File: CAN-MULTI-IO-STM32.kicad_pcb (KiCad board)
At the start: 2 copper layers, 81 x 55 mm, 63 parts, among them J1 H GND L, J2 TERM, J3 USART1, J5 PWR IN, U1 STM32L433RCT3, U2 MCP2562-E-SN, U3 LMR54410, U4 ADS1015IDGS, U5 PCA9537, U6 TCA9511

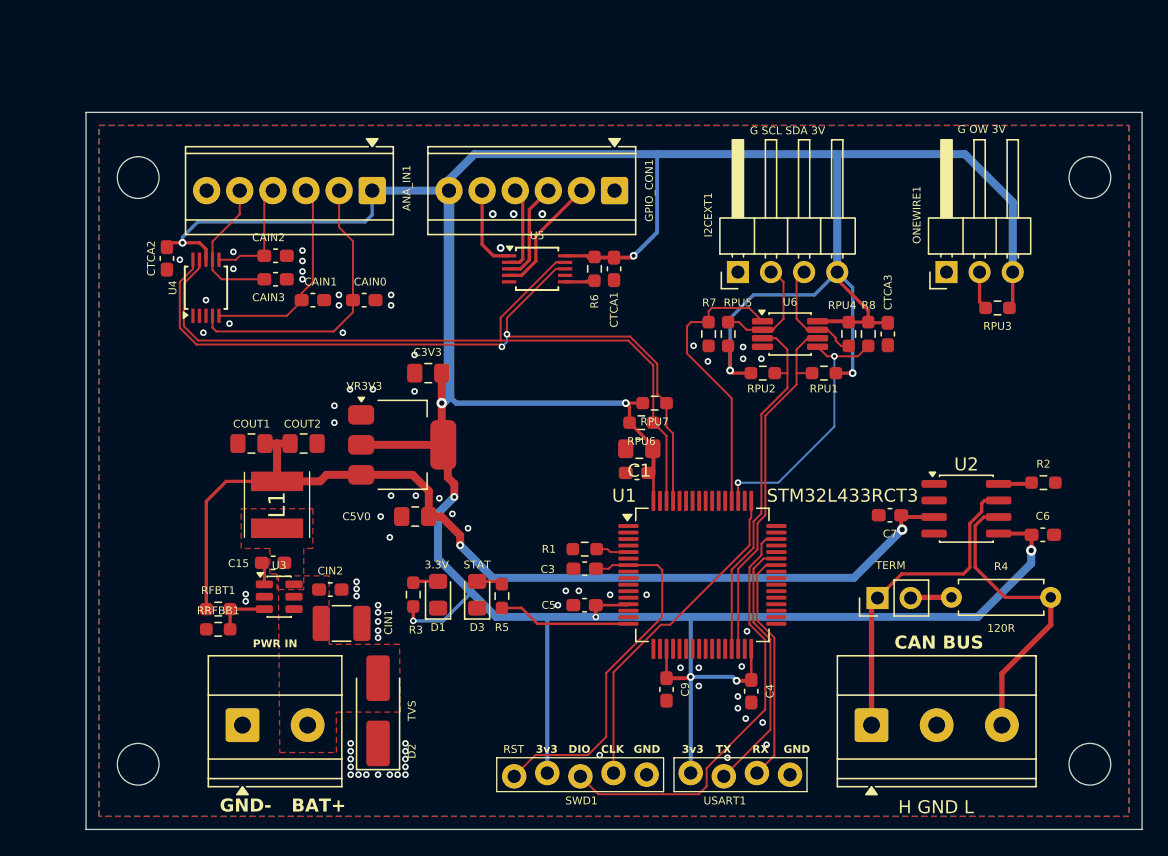
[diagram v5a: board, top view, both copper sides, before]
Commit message: first pass layout complete
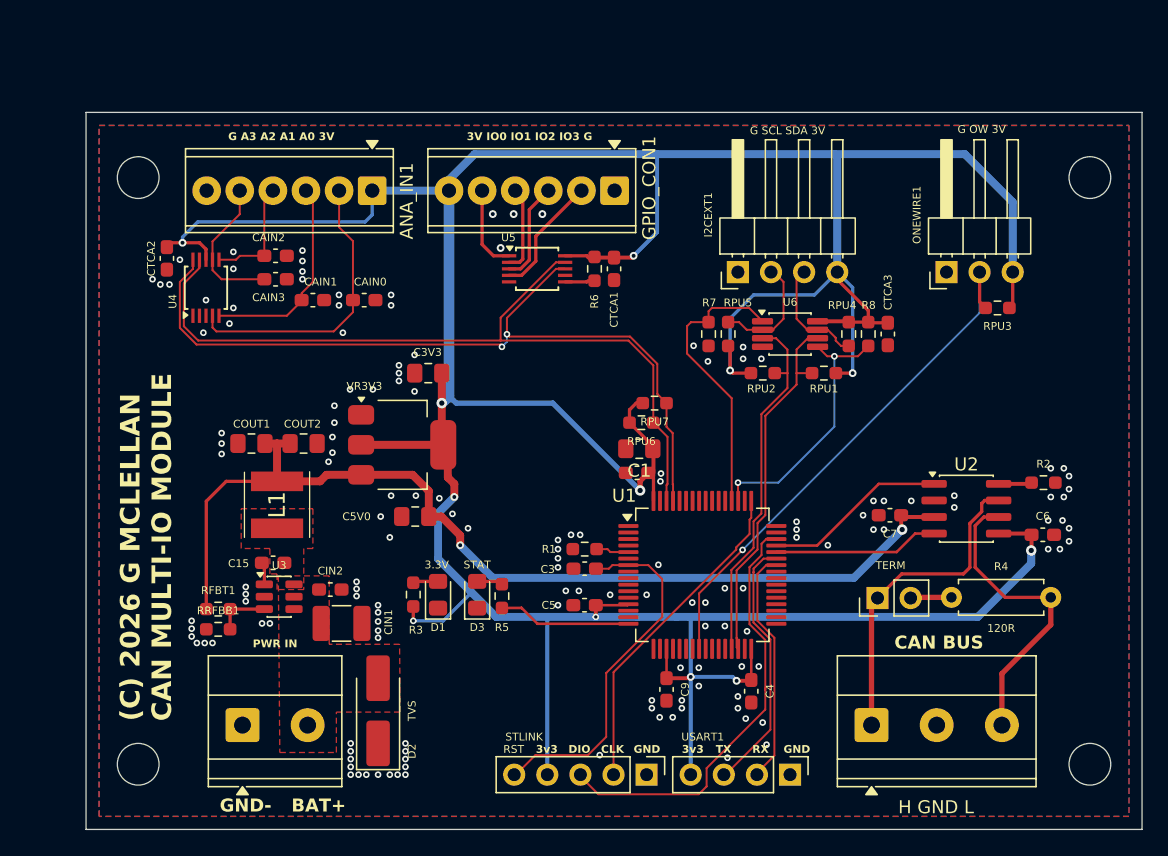
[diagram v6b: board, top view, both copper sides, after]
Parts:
- ANA_IN1, GPIO_CON1: footprint TerminalBlock_TE-Connectivity:TerminalBlock_TE_282834-6_1x06_P2.54mm_Horizontal -> TerminalBlock_Phoenix:TerminalBlock_Phoenix_MPT-0,5-6-2.54_1x06_P2.54mm_Horizontal
- J3: footprint PCM_SparkFun-Connector:1x04_P2.54mm_Locking -> Connector_PinHeader_2.54mm:PinHeader_1x04_P2.54mm_Vertical
- SWD1: footprint PCM_SparkFun-Connector:1x05_P2.54mm_Locking -> Connector_PinHeader_2.54mm:PinHeader_1x05_P2.54mm_Vertical
- turned J3 to -90 degrees
- turned SWD1 to -90 degrees
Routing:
- net /ONEW: track 2.94 -> 40.8 mm, vias 0 -> 1
- net /CAN1_TX: track 0.00 -> 14.1 mm
- net /CAN1_RX: track 0.00 -> 12.7 mm
- net +3.3V: track 303.2 -> 308.3 mm
- net GND: vias 79 -> 147
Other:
- board text added: "(C) 2026 G MCLELLAN CAN MULTI-IO MODULE"
- board text added: "3V IO0 IO1 IO2 IO3 G"
- board text added: "G A3 A2 A1 A0 3V"
- board text removed: "(C) 2026 G MCLELLAN CAN MULTI-IO INTERFACE REV 01"

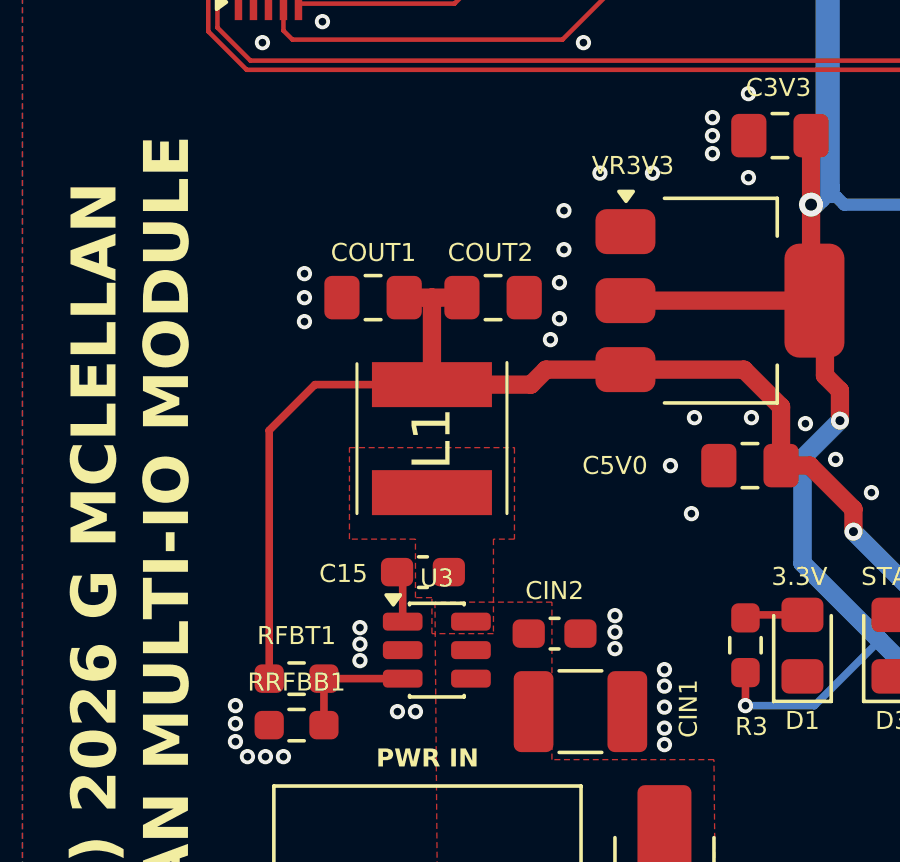
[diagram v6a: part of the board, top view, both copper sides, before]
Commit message: fixed issue with incorrect inductor
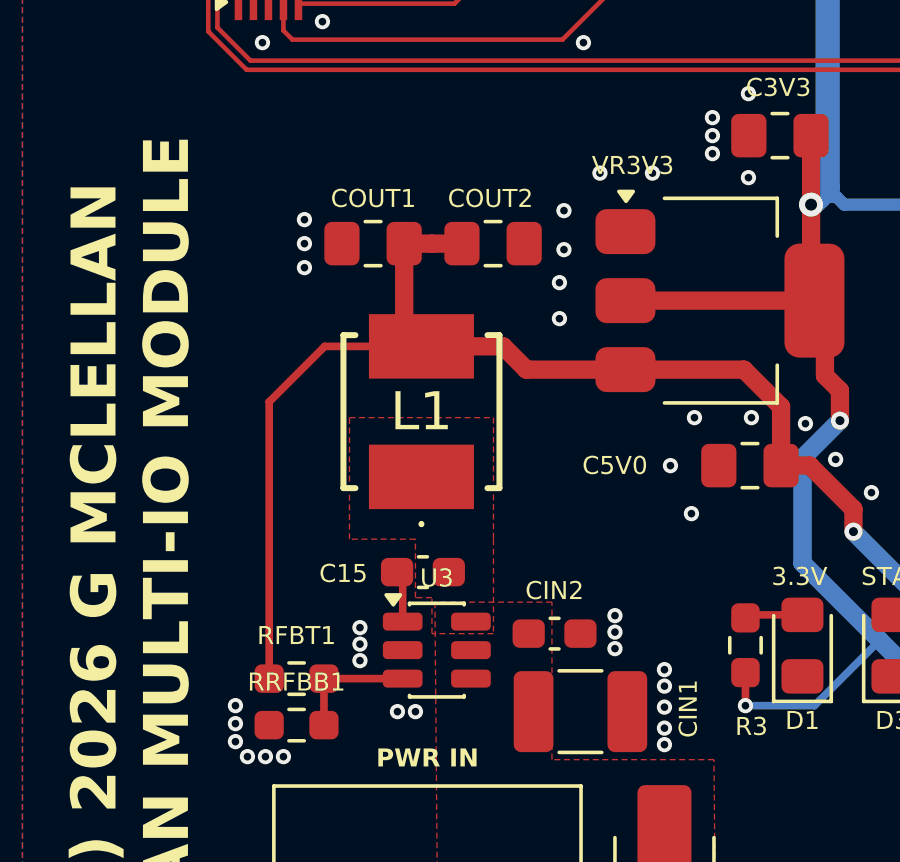
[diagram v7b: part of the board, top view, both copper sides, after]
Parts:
- L1: value VLS5045EX-100M-H -> SRP5030HMT-8R2M; footprint SamacSys_Parts:VLS5045EX330M -> SamacSys_Parts:SRP5030HMT2R2M
- moved COUT1 1.80 mm to (109.7, 98.6)
- moved COUT2 1.80 mm to (113.7, 98.6)
- moved L1 0.97 mm to (111.3, 104.2), turned to 0 degrees
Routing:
- net +5V: track 77.4 -> 79.4 mm
- net GND: vias 147 -> 146

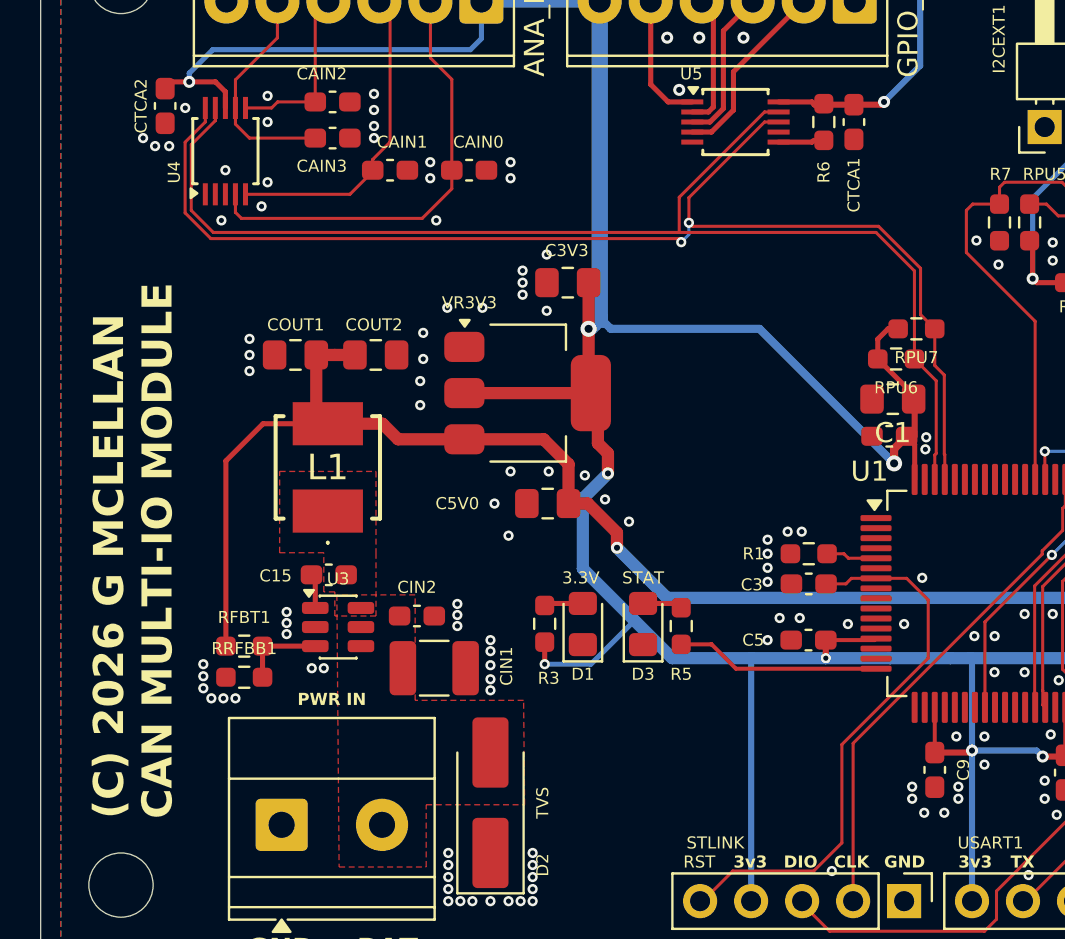
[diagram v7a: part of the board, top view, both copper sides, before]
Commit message: silkscreen cleanup
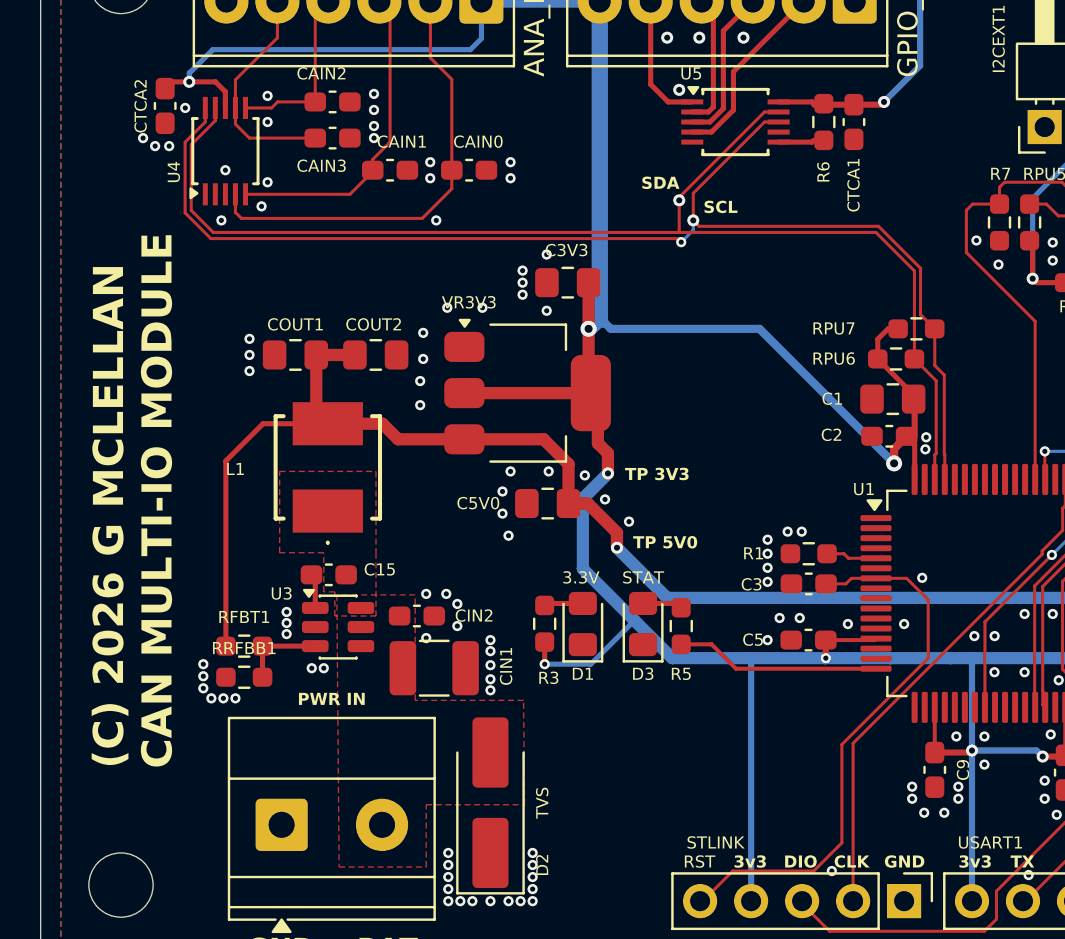
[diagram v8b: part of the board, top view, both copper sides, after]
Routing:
- net GND: vias 146 -> 149
- net /I2C1_SDA: vias 0 -> 1
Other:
- board text added: "SCL"
- board text added: "SDA"
- board text added: "TP 3V3"
- board text added: "TP 5V0"
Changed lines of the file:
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@@
 		(tags "capacitor handsolder")
 		(property "Reference" "C5V0"
-			(at 4.5 0 0)
+			(at 3.45 0 0)
 			(layer "F.SilkS")
 			(effects
@@
 		(tags "capacitor handsolder")
 		(property "Reference" "C1"
-			(at 0 -1.68 0)
+			(at 3 0 0)
 			(layer "F.SilkS")
 			(effects
 				(font
-					(size 1 1)
-					(thickness 0.15)
+					(size 0.6 0.6)
+					(thickness 0.1)
 				)
 			)
@@
 		(tags "resistor handsolder")
 		(property "Reference" "RPU7"
-			(at 0 -1.43 0)
+			(at 4.1125 0 0)
 			(layer "F.SilkS")
 			(effects
@@
 		(tags "capacitor handsolder")
 		(property "Reference" "C15"
-			(at -2.65 0.05 0)
+			(at 2.55 -0.25 0)
 			(layer "F.SilkS")
 			(effects
@@
 		(tags "capacitor handsolder")
 		(property "Reference" "C2"
-			(at 2.6875 0.05 0)
+			(at 2.8625 0.05 0)
 			(layer "F.SilkS")
-			(hide yes)
 			(effects
 				(font
-					(size 1 1)
-					(thickness 0.15)
+					(size 0.6 0.6)
+					(thickness 0.1)
 				)
 			)
@@
 		(tags "resistor handsolder")
 		(property "Reference" "RPU6"
-			(at 0 -1.43 0)
+			(at 3.1 0 0)
 			(layer "F.SilkS")
 			(effects
@@
 		(tags "LQFP QFP")
 		(property "Reference" "U1"
-			(at -6 -6.075 0)
+			(at -6.275 -5.175 0)
 			(layer "F.SilkS")
 			(effects
 				(font
-					(size 1 1)
-					(thickness 0.15)
+					(size 0.6 0.6)
+					(thickness 0.1)
 				)
 			)
@@
 		(tags "Inductor")
 		(property "Reference" "L1"
-			(at 0 0 0)
+			(at -4.6 0.1 0)
 			(layer "F.SilkS")
 			(effects
 				(font
-					(size 1.27 1.27)
-					(thickness 0.254)
+					(size 0.6 0.6)
+					(thickness 0.1)
 				)
 			)
@@
 		(tags "capacitor handsolder")
 		(property "Reference" "CIN2"
-			(at 0 -1.43 0)
+			(at 2.8625 0 0)
 			(layer "F.SilkS")
 			(effects
@@
 		(tags "SOT TO_SOT_SMD")
 		(property "Reference" "U3"
-			(at 0 -2.4 0)
+			(at -2.8125 -1.65 0)
 			(layer "F.SilkS")
 			(effects
@@
 		)
 	)
+	(gr_text "SCL"
+		(at 130 91.6 0)
+		(layer "F.SilkS")
+		(effects
+			(font
+				(size 0.6 0.6)
+				(thickness 0.1)
+				(bold yes)
+			)
+			(justify left bottom)
+		)
+	)
+	(gr_text "SDA"
+		(at 126.9 90.4 0)
+		(layer "F.SilkS")
+		(effects
+			(font
+				(size 0.6 0.6)
+				(thickness 0.1)
+				(bold yes)
+			)
+			(justify left bottom)
+		)
+	)
 	(gr_text "TX"
 		(at 145.3 124.2 0)
@@
 	)
 	(gr_text "(C) 2026 G MCLELLAN\nCAN MULTI-IO MODULE"
-		(at 103.7 121.7 90)
+		(at 103.7 119.2 90)
 		(layer "F.SilkS")
 		(effects
@@
 		)
 	)
+	(gr_text "TP 3V3"
+		(at 126.1 104.9 0)
+		(layer "F.SilkS")
+		(effects
+			(font
+				(size 0.6 0.6)
+				(thickness 0.1)
+				(bold yes)
+			)
+			(justify left bottom)
+		)
+	)
 	(gr_text "GND-"
 		(at 107.25 128.75 0)
@@
 		)
 	)
+	(gr_text "TP 5V0"
+		(at 126.5 108.3 0)
+		(layer "F.SilkS")
+		(effects
+			(font
+				(size 0.6 0.6)
+				(thickness 0.1)
+				(bold yes)
+			)
+			(justify left bottom)
+		)
+	)
 	(gr_text "3V IO0 IO1 IO2 IO3 G"
 		(at 126.2 77.2 0)
@@
 	)
 	(via
+		(at 116.2 110.5)
+		(size 0.508)
+		(drill 0.254)
+		(layers "F.Cu" "B.Cu")
+		(free yes)
+		(net 6)
+	)
+	(via
 		(at 121.5 125.8)
 		(size 0.508)
@@
 	)
 	(via
+		(at 116.2 112.7)
+		(size 0.508)
+		(drill 0.254)
+		(layers "F.Cu" "B.Cu")
+		(free yes)
+		(net 6)
+	)
+	(via
 		(at 120.3 125.8)
 		(size 0.508)
@@
 	)
 	(via
+		(at 117.2 110.5)
+		(size 0.508)
+		(drill 0.254)
+		(layers "F.Cu" "B.Cu")
+		(free yes)
+		(net 6)
+	)
+	(via
 		(at 109.25 112.5)
 		(size 0.508)
@@
 	)
 	(via
-		(at 117.75 111.55)
+		(at 117.3 123.4)
 		(size 0.508)
 		(drill 0.254)
@@
 	)
 	(via
-		(at 117.3 123.4)
+		(at 142.7 120.7)
 		(size 0.508)
 		(drill 0.254)
@@
 	)
 	(via
-		(at 142.7 120.7)
+		(at 147.3 117.5)
 		(size 0.508)
 		(drill 0.254)
@@
 	)
 	(via
-		(at 147.3 117.5)
+		(at 121.5 124)
 		(size 0.508)
 		(drill 0.254)
@@
 	)
 	(via
-		(at 121.5 124)
+		(at 120 105.4)
 		(size 0.508)
 		(drill 0.254)
@@
 	)
 	(via
-		(at 119.6 106)
+		(at 120 106.5)
 		(size 0.508)
 		(drill 0.254)
@@
 	(segment
 		(start 128.8 90.7476)
-		(end 128.8 92.5)
+		(end 128.8 90.9)
 		(width 0.1524)
 		(layer "F.Cu")
@@
 	)
 	(segment
+		(start 128.8 90.9)
+		(end 128.8 92.5)
+		(width 0.1524)
+		(layer "F.Cu")
+		(net 65)
+	)
+	(segment
 		(start 105.7 86.3)
 		(end 105.7 86.932466)
@@
 		(net 65)
 	)
+	(via
+		(at 128.8 90.9)
+		(size 0.6)
+		(drill 0.3)
+		(layers "F.Cu" "B.Cu")
+		(tenting none)
+		(net 65)
+	)
 	(segment
 		(start 142 99.6)
@@
 	)
 	(segment
-		(start 105.473333 92.8058)
-		(end 104.1942 91.526667)
-		(width 0.1524)
-		(layer "F.Cu")
-		(net 66)
-	)
-	(segment
-		(start 140.8183 94.285833)
-		(end 140.8183 96.5933)
-		(width 0.1524)
-		(layer "F.Cu")
-		(net 66)
-	)
-	(segment
-		(start 129.2826 90.765)
+		(start 129.5 90.5476)
 		(end 133.0476 87)
 		(width 0.1524)
@@
 	)
 	(segment
-		(start 129.4594 92.1942)
+		(start 129.7942 92.1942)
 		(end 138.726666 92.1942)
 		(width 0.1524)
@@
 	)
 	(segment
-		(start 128.9 92.9826)
-		(end 128.9 92.9)
+		(start 105.473333 92.8058)
+		(end 104.1942 91.526667)
 		(width 0.1524)
 		(layer "F.Cu")
@@
 	)
 	(segment
-		(start 129.2826 92.0174)
-		(end 129.2826 90.765)
+		(start 133.0476 87)
+		(end 133.75 87)
 		(width 0.1524)
 		(layer "F.Cu")
@@
 	)
 	(segment
-		(start 138.726666 92.1942)
-		(end 140.8183 94.285833)
+		(start 128.9 92.9826)
+		(end 128.9 92.9)
 		(width 0.1524)
 		(layer "F.Cu")
@@
 	)
 	(segment
-		(start 133.0476 87)
-		(end 133.75 87)
+		(start 129.5 91.9)
+		(end 129.7942 92.1942)
 		(width 0.1524)
 		(layer "F.Cu")
@@
 	)
 	(segment
+		(start 138.726666 92.1942)
+		(end 140.8183 94.285833)
+		(width 0.1524)
+		(layer "F.Cu")
+		(net 66)
+	)
+	(segment
+		(start 129.5 91.9)
+		(end 129.5 90.5476)
+		(width 0.1524)
+		(layer "F.Cu")
+		(net 66)
+	)
+	(segment
 		(start 128.9 92.9)
 		(end 128.8058 92.8058)
@@
 	)
 	(segment
-		(start 129.2826 92.0174)
-		(end 129.4594 92.1942)
+		(start 140.8183 94.285833)
+		(end 140.8183 96.5933)
 		(width 0.1524)
 		(layer "F.Cu")
@@
 	)
 	(via
-		(at 129.2826 92.0174)
-		(size 0.508)
-		(drill 0.254)
+		(at 129.5 91.9)
+		(size 0.6)
+		(drill 0.3)
 		(layers "F.Cu" "B.Cu")
+		(tenting none)
 		(net 66)
 	)
 	(segment
-		(start 129.2826 92.6)
-		(end 128.9 92.9826)
+		(start 129.5 91.9)
+		(end 129.5 92.3826)
 		(width 0.1524)
 		(layer "B.Cu")
@@
 	)
 	(segment
-		(start 129.2826 92.0174)
-		(end 129.2826 92.6)
+		(start 129.5 92.3826)
+		(end 128.9 92.9826)
 		(width 0.1524)
 		(layer "B.Cu")
